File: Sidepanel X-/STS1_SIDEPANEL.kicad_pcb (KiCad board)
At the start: 2 copper layers, 82.8 x 100 mm, 30 parts, among them IC1 TMP112AQDRLRQ1, J1 Conn_02x04_Odd_Even, J2 Conn_02x02_Odd_Even, U1 GUVA-C32SM

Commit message: Review Ready for V2.0
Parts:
- CUR1: footprint SamacSys:SOIC127P600X175-8N -> Package_SO:SOIC-8_3.9x4.9mm_P1.27mm
- DOUT1: footprint SamacSys:STMITE -> Diode_SMD:D_0603_1608Metric
- IC1: footprint SamacSys:SOTFL50P160X60-6N -> Package_TO_SOT_SMD:SOT-563
- J1: footprint SamacSys:M808280842 -> STS_Connector:M808280842
- J2: footprint USER_Passiv:M80-8280442 -> STS_Connector:M808280442
- L_IN1: footprint SamacSys:INDPM5650X530N -> Inductor_SMD:L_0805_2012Metric
- MPPT1: footprint SamacSys:SOP65P640X120-8N -> Package_SO:TSSOP-8_4.4x3mm_P0.65mm
- U1: footprint USER_Optic:OLGA 2mm x 2,3mm -> Package_SO:SO-4_4.4x3.6mm_P2.54mm
- moved J2 66.8 mm to (147.4, 60.3), turned to 180 degrees
- moved C2 54.2 mm to (155.5, 69.1)
- moved C1 53.7 mm to (155.5, 73.4)
- moved RIC1 53.1 mm to (148.5, 68.1)
- moved RIC2 53.1 mm to (148.5, 70.1)
- moved RU1 53.1 mm to (148.5, 74.4)
- moved RU2 53.1 mm to (148.5, 72.4)
- moved IC1 51.7 mm to (152.5, 71.7)
- moved U1 49.4 mm to (141.5, 69.8)
- moved SC1 23.6 mm to (125.0, 109.2), turned to 0 degrees
- moved J1 16.1 mm to (135.0, 60.3), turned to 180 degrees
- moved C_IN1 2.13 mm to (129.1, 77.2)
- moved CUR1 2.13 mm to (124.4, 81.2)
- moved C_CUR11 2.02 mm to (123.4, 86.7)
- moved C_CUR21 2.02 mm to (123.4, 88.5)
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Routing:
- net /MPPT1: track 127.5 -> 89.2 mm, vias 4 -> 1
- net /SC1_V+: track 32.0 -> 52.3 mm, vias 7 -> 2
- net /SCL: track 17.8 -> 33.9 mm, vias 1 -> 2
- net /Sensors/VBAT: track 2.06 -> 16.1 mm
- net /SolarMPPT/CUR1_OUT: track 0.00 -> 12.5 mm
- net /+3V3: track 33.2 -> 23.2 mm
- net /SDA: track 18.5 -> 26.0 mm, vias 1 -> 2
- net GND: track 6.50 -> 12.6 mm, vias 282 -> 262
- net /SC1_I+: track 38.6 -> 35.1 mm, vias 2 -> 0
- net /SC2_V+: track 1.60 -> 0.00 mm
- net /SolarMPPT/MPPT1_IN: track 6.57 -> 7.17 mm
- removed copper zone on B.Cu, net /SC1_V+
- removed copper zone on F.Cu, net /SC1_V+
- removed copper zone on B.Cu, net /SolarMPPT/CUR1_OUT
- removed copper zone on B.Cu, net /SolarMPPT/MPPT1_IN
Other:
- outline, holes or cut-outs redrawn

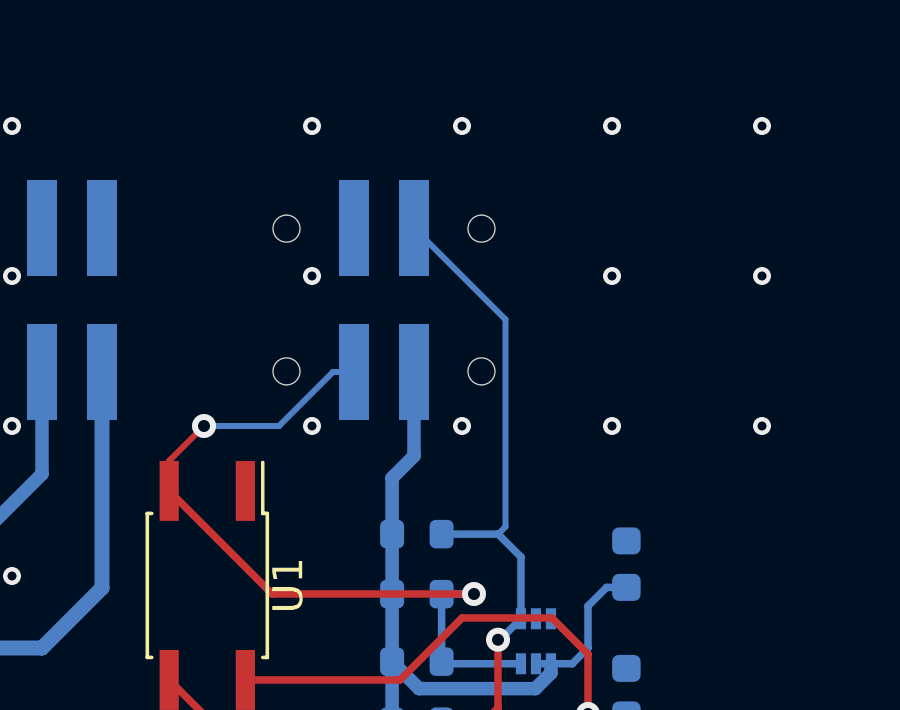
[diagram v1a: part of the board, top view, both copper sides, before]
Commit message: Paar Fehler behoben, Z+ no MOSFET
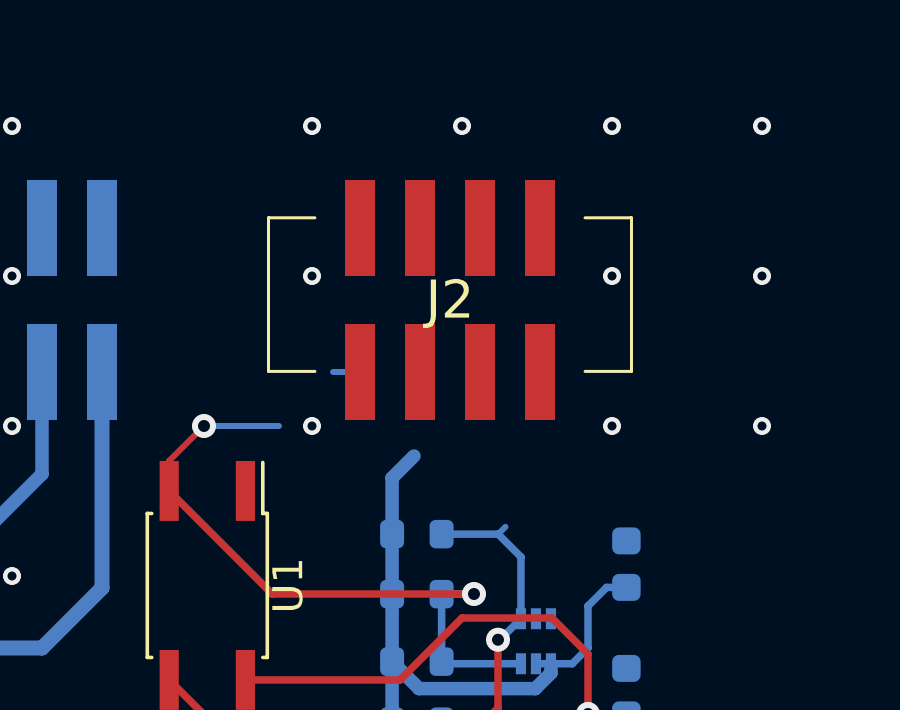
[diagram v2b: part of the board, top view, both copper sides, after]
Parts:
- J2: value Conn_02x02_Odd_Even -> Conn_02x04_Odd_Even; footprint STS_Connector:M808280442 -> STS_Connector:M808280842; moved to F.Cu
- moved J2 2.20 mm to (149.6, 60.3)
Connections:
- C1 pad 1: /Sensors/VBAT -> VBAT
- J2 pad 1: /+3V3 -> VBAT
- J2 pad 2: /SDA -> unconnected-(J2-Pad2)
- J2 pad 3: /SCL -> unconnected-(J2-Pad3)
- J2 pad 4: GND -> unconnected-(J2-Pad4)
- U1 pad 4: /Sensors/VBAT -> VBAT
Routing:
- net VBAT: track 0.00 -> 16.1 mm, vias 0 -> 1
- net /Sensors/VBAT: track 16.1 -> 0.00 mm, vias 1 -> 0
- net /SCL: track 33.9 -> 22.6 mm
- net /+3V3: track 23.2 -> 20.4 mm
- net /SDA: track 26.0 -> 23.4 mm
- net GND: vias 262 -> 261

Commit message: Further fixes, still some open
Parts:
- J2: value Conn_02x04_Odd_Even -> Conn_02x02_Odd_Even; footprint STS_Connector:M808280842 -> STS_Connector:M808280442; moved to B.Cu
- moved J2 0.40 mm to (150.0, 60.3)
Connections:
- C1 pad 1: VBAT -> /+3V3
- J2 pad 1: VBAT -> /+3V3
- J2 pad 2: unconnected-(J2-Pad2) -> /SDA
- J2 pad 3: unconnected-(J2-Pad3) -> /SCL
- J2 pad 4: unconnected-(J2-Pad4) -> GND
- U1 pad 4: VBAT -> /+3V3
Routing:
- net /+3V3: track 20.4 -> 41.4 mm, vias 0 -> 1
- net VBAT: track 16.1 -> 0.00 mm, vias 1 -> 0
- net /SCL: track 22.6 -> 33.6 mm
- net /SDA: track 23.4 -> 28.6 mm
- net /SolarMPPT/MPPT1_OUT: track 14.9 -> 19.1 mm
- net /MPPT1: track 89.2 -> 88.2 mm, vias 1 -> 0
- net GND: vias 261 -> 260

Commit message: Next fix
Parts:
- added TH1: Thermistor_NTC, Resistor_SMD:R_0805_2012Metric_Pad1.20x1.40mm_HandSolder, B.Cu at (139.0, 51.9)
- SC1: footprint USER_Activ:3G30A_40x80 -> STS_Solarcells:3G30A_40x80
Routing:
- net /SC1_V+: track 52.3 -> 249.5 mm
- net GND: track 12.6 -> 58.8 mm, vias 260 -> 193
- net /TEMP+: track 0.00 -> 6.00 mm
- net /+3V3: track 41.4 -> 43.6 mm

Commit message: release_2.0, Ordered PCBs
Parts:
- DOUT1: footprint Diode_SMD:D_0603_1608Metric -> SamacSys:STMITE
- L_IN1: footprint Inductor_SMD:L_0805_2012Metric -> STS_Inductor_SMD:XAL6060103MEC
- moved DOUT1 5.29 mm to (137.4, 80.3), turned to 90 degrees
- moved L_IN1 2.67 mm to (131.6, 80.6)
- moved C_IN1 2.61 mm to (127.9, 74.9)
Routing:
- net GND: track 58.8 -> 50.1 mm, vias 193 -> 191
- net /SC1_V+: track 249.5 -> 242.5 mm
- net /SolarMPPT/CUR1_OUT: track 12.5 -> 15.4 mm
- net /SolarMPPT/MPPT1_IN: track 7.17 -> 7.93 mm

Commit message: Diode D1 angebracht
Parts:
- added D1: PMEG2020EH, Diode_SMD:D_SOD-123F, B.Cu at (136.4, 74.3)
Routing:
- net /SolarMPPT/MPPT1_OUT: track 19.1 -> 28.2 mm
- net /SolarMPPT/MPPT1_IN: track 7.93 -> 14.9 mm
- net GND: vias 191 -> 190
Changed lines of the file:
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@@
     (pad_to_mask_clearance 0)
     (aux_axis_origin 125 89.5)
-    (grid_origin 125 89.5)
+    (grid_origin 131.35 83.15)
     (pcbplotparams
       (layerselection 0x00010fc_ffffffff)
@@
       (net 1 "GND") (pintype "passive"))
     (model "${KICAD6_3DMODEL_DIR}/Capacitor_SMD.3dshapes/C_0603_1608Metric.wrl"
+      (offset (xyz 0 0 0))
+      (scale (xyz 1 1 1))
+      (rotate (xyz 0 0 0))
+    )
+  )
+  (footprint "Diode_SMD:D_SOD-123F" (layer "B.Cu")
+    (at 136.43 74.26 180)
+    (descr "D_SOD-123F")
+    (tags "D_SOD-123F")
+    (property "Sheetfile" "SolarMPPT.kicad_sch")
+    (property "Sheetname" "SolarMPPT")
+    (attr smd)
+    (fp_text reference "D1" (at -0.127 1.905) (layer "B.SilkS")
+      (effects (font (size 1 1) (thickness 0.15)) (justify mirror))
+    )
+    (fp_text value "PMEG2020EH" (at 0 -2.1) (layer "B.Fab")
+      (effects (font (size 1 1) (thickness 0.15)) (justify mirror))
+    )
+    (fp_text user "${REFERENCE}" (at -0.127 1.905) (layer "B.Fab")
+      (effects (font (size 1 1) (thickness 0.15)) (justify mirror))
+    )
+    (fp_line (start -2.2 -1) (end 1.65 -1) (layer "B.SilkS") (width 0.12))
+    (fp_line (start -2.2 1) (end 1.65 1) (layer "B.SilkS") (width 0.12))
+    (fp_line (start -2.2 1) (end -2.2 -1) (layer "B.SilkS") (width 0.12))
+    (fp_line (start 2.2 1.15) (end 2.2 -1.15) (layer "B.CrtYd") (width 0.05))
+    (fp_line (start -2.2 1.15) (end -2.2 -1.15) (layer "B.CrtYd") (width 0.05))
+    (fp_line (start 2.2 -1.15) (end -2.2 -1.15) (layer "B.CrtYd") (width 0.05))
+    (fp_line (start -2.2 1.15) (end 2.2 1.15) (layer "B.CrtYd") (width 0.05))
+    (fp_line (start -1.4 0.9) (end 1.4 0.9) (layer "B.Fab") (width 0.1))
+    (fp_line (start 0.25 0) (end 0.75 0) (layer "B.Fab") (width 0.1))
+    (fp_line (start -0.35 0) (end -0.35 -0.55) (layer "B.Fab") (width 0.1))
+    (fp_line (start -0.35 0) (end 0.25 0.4) (layer "B.Fab") (width 0.1))
+    (fp_line (start 1.4 -0.9) (end -1.4 -0.9) (layer "B.Fab") (width 0.1))
+    (fp_line (start 0.25 -0.4) (end -0.35 0) (layer "B.Fab") (width 0.1))
+    (fp_line (start -0.35 0) (end -0.35 0.55) (layer "B.Fab") (width 0.1))
+    (fp_line (start 1.4 0.9) (end 1.4 -0.9) (layer "B.Fab") (width 0.1))
+    (fp_line (start 0.25 0.4) (end 0.25 -0.4) (layer "B.Fab") (width 0.1))
+    (fp_line (start -0.75 0) (end -0.35 0) (layer "B.Fab") (width 0.1))
+    (fp_line (start -1.4 -0.9) (end -1.4 0.9) (layer "B.Fab") (width 0.1))
+    (pad "1" smd rect (at -1.4 0 180) (size 1.1 1.1) (layers "B.Cu" "B.Paste" "B.Mask")
+      (net 18 "/SolarMPPT/MPPT1_OUT") (pinfunction "K") (pintype "passive"))
+    (pad "2" smd rect (at 1.4 0 180) (size 1.1 1.1) (layers "B.Cu" "B.Paste" "B.Mask")
+      (net 20 "/SolarMPPT/MPPT1_IN") (pinfunction "A") (pintype "passive"))
+    (model "${KICAD6_3DMODEL_DIR}/Diode_SMD.3dshapes/D_SOD-123F.wrl"
       (offset (xyz 0 0 0))
       (scale (xyz 1 1 1))
@@
   (via (at 115 59.5) (size 0.6) (drill 0.3) (layers "F.Cu" "B.Cu") (free) (net 1))
   (via (at 90 109.5) (size 0.6) (drill 0.3) (layers "F.Cu" "B.Cu") (free) (net 1))
-  (via (at 135 74.5) (size 0.6) (drill 0.3) (layers "F.Cu" "B.Cu") (free) (net 1))
   (via (at 105 79.5) (size 0.6) (drill 0.3) (layers "F.Cu" "B.Cu") (free) (net 1))
   (via (at 85 94.5) (size 0.6) (drill 0.3) (layers "F.Cu" "B.Cu") (free) (net 1))
@@
   (segment (start 127.2 96.5) (end 127.2 89.9) (width 0.5) (layer "B.Cu") (net 18))
   (segment (start 134 90) (end 134.925 90) (width 0.45) (layer "B.Cu") (net 18))
+  (segment (start 130.75 99.075) (end 129.775 99.075) (width 0.5) (layer "B.Cu") (net 18))
   (segment (start 134.925 90) (end 135 89.925) (width 0.45) (layer "B.Cu") (net 18))
+  (segment (start 139.713 79.867) (end 140.24 79.34) (width 0.75) (layer "B.Cu") (net 18))
   (segment (start 129.775 99.075) (end 127.2 96.5) (width 0.5) (layer "B.Cu") (net 18))
-  (segment (start 130.75 99.075) (end 129.775 99.075) (width 0.5) (layer "B.Cu") (net 18))
+  (segment (start 137.4 79.867) (end 139.713 79.867) (width 0.75) (layer "B.Cu") (net 18))
+  (segment (start 140.24 76.67) (end 137.83 74.26) (width 0.75) (layer "B.Cu") (net 18))
+  (segment (start 140.24 79.34) (end 140.24 76.67) (width 0.75) (layer "B.Cu") (net 18))
   (segment (start 127.125 74.9) (end 127.125 77.885) (width 1) (layer "B.Cu") (net 19))
   (segment (start 129 86.175) (end 129 81.18) (width 1) (layer "B.Cu") (net 19))
@@
   (segment (start 127.125 77.885) (end 126.27 78.74) (width 1) (layer "B.Cu") (net 19))
   (segment (start 128.13 80.6) (end 126.27 78.74) (width 1) (layer "B.Cu") (net 19))
-  (segment (start 132.075 82.145) (end 133.62 80.6) (width 0.3) (layer "B.Cu") (net 20))
-  (segment (start 132.075 87.8875) (end 132.075 82.145) (width 0.3) (layer "B.Cu") (net 20))
+  (segment (start 132.075 87.8875) (end 132.075 85.145) (width 0.45) (layer "B.Cu") (net 20))
+  (segment (start 132.075 85.145) (end 132.075 82.145) (width 0.45) (layer "B.Cu") (net 20))
+  (segment (start 135.03 74.26) (end 135.03 79.19) (width 0.75) (layer "B.Cu") (net 20))
+  (segment (start 132.075 82.145) (end 133.62 80.6) (width 0.45) (layer "B.Cu") (net 20))
+  (segment (start 135.03 79.19) (end 133.62 80.6) (width 0.75) (layer "B.Cu") (net 20))
   (zone locked (net 1) (net_name "GND") (layers F&B.Cu) (hatch edge 0.508)
     (connect_pads (clearance 0.2))
